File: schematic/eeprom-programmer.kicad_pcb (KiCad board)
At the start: 2 copper layers, 39.6 x 69.1 mm, 8 parts, among them IC1 AT28C64B-15PU, U1 74HC595, U2 74HC595

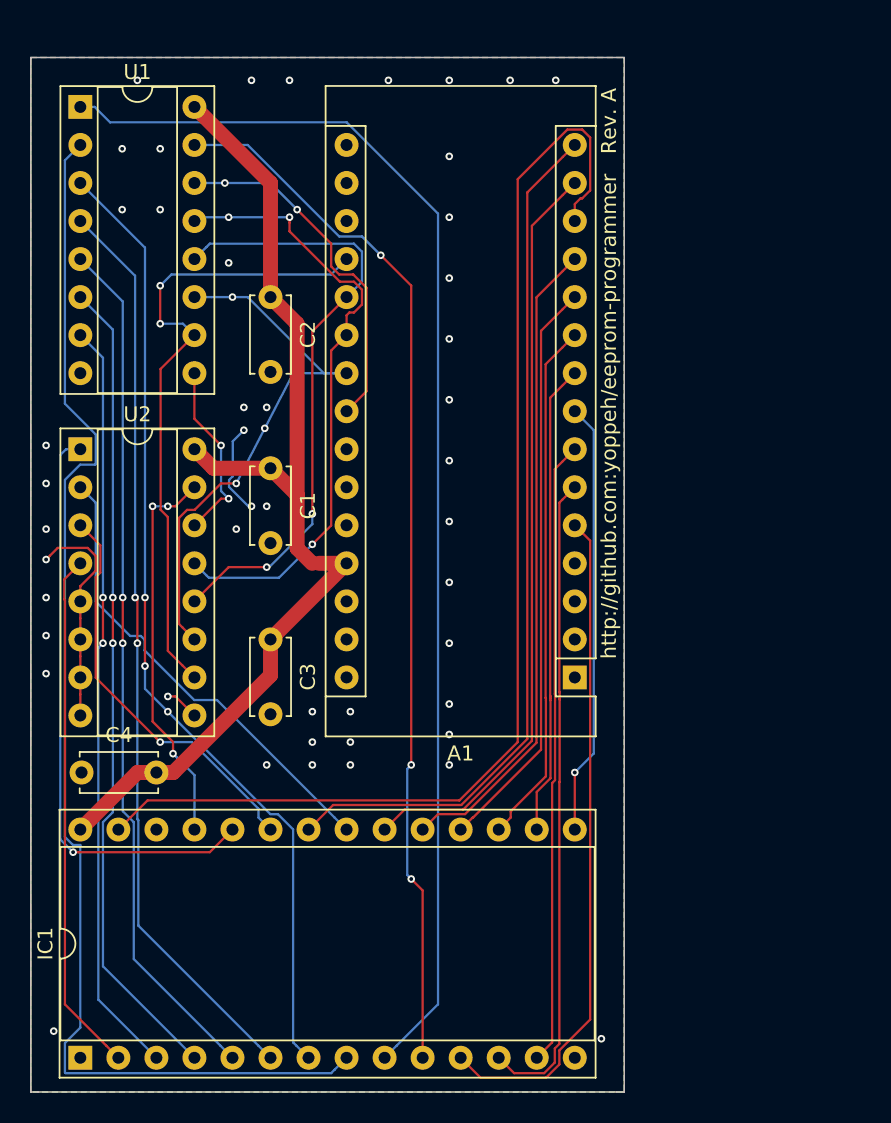
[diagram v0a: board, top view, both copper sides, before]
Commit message: Update PCB layout to handle up to 32kx8 eeproms
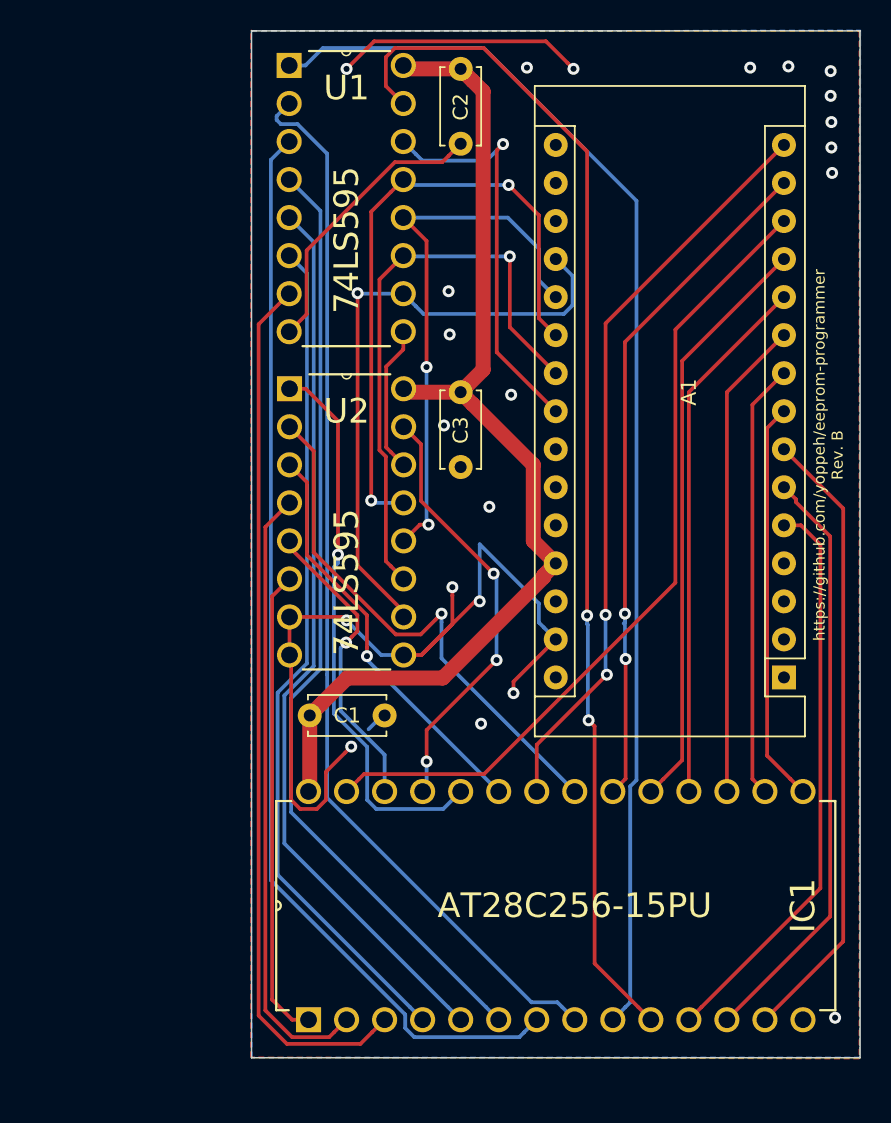
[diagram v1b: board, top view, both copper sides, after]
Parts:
- removed C4: .1uF, Capacitor_THT:C_Disc_D5.0mm_W2.5mm_P5.00mm
- A1: footprint Module:Arduino_Nano -> eeprom-programmer:Arduino_Nano
- C1, C2, C3: value .1uF -> .1uf; footprint Capacitor_THT:C_Disc_D5.0mm_W2.5mm_P5.00mm -> eeprom-programmer:C_Disc_D5.0mm_W2.5mm_P5.00mm
- IC1: value AT28C64B-15PU -> AT28C256-15PU; footprint Package_DIP:DIP-28_W15.24mm_Socket -> eeprom-programmer:DIP254P1524X482-28
- U1, U2: value 74HC595 -> 74LS595; footprint Package_DIP:DIP-16_W7.62mm_Socket -> eeprom-programmer:DIP254P762X508-16
- moved IC1 51.4 mm to (143.5, 115.6)
- moved U1 26.3 mm to (116.8, 84.9)
- moved U2 25.6 mm to (116.8, 106.5)
- moved C1 18.2 mm to (115.6, 110.5), turned to 180 degrees
- moved C3 17.1 mm to (120.7, 93.9), turned to 90 degrees
- moved C2 16.3 mm to (120.7, 72.3), turned to 90 degrees
- moved A1 14.0 mm to (142.2, 108.0)
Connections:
- A1 pad 1: (no net) -> Net-(A1-Pad1)
- A1 pad 16: (no net) -> Net-(A1-Pad16)
- A1 pad 17: (no net) -> Net-(A1-Pad17)
- A1 pad 18: (no net) -> Net-(A1-Pad18)
- A1 pad 2: (no net) -> Net-(A1-Pad2)
- A1 pad 24: (no net) -> Net-(A1-Pad24)
- A1 pad 25: (no net) -> Net-(A1-Pad25)
- A1 pad 26: (no net) -> Net-(A1-Pad26)
- A1 pad 28: (no net) -> Net-(A1-Pad28)
- A1 pad 3: (no net) -> Net-(A1-Pad3)
- A1 pad 30: (no net) -> Net-(A1-Pad30)
- A1 pad 4: (no net) -> Net-(A1-Pad4)
- C1 pad 1: Arduino5V -> GND
- C1 pad 2: GND -> Arduino5V
- C2 pad 1: Arduino5V -> GND
- C2 pad 2: GND -> Arduino5V
- C3 pad 1: Arduino5V -> GND
- C3 pad 2: GND -> Arduino5V
- IC1 pad 1: (no net) -> /addr14
- IC1 pad 26: (no net) -> /addr13
- U2 pad 5: GND -> /addr13
- U2 pad 6: GND -> /addr14
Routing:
- net GND: track 23.5 -> 94.3 mm, vias 47 -> 22
- net /addr14: track 0.00 -> 31.6 mm
- net eeNotWriteEnable: track 79.2 -> 54.9 mm
- net /addr13: track 0.00 -> 20.3 mm, vias 0 -> 1
- net /addr02: track 85.1 -> 71.4 mm
- net /addr00: track 70.5 -> 79.9 mm, vias 3 -> 2
- net /addr07: track 50.6 -> 58.9 mm, vias 2 -> 0
- net eeNotOutputEnable: track 58.1 -> 50.1 mm, vias 0 -> 2
- net /addr03: track 65.0 -> 72.9 mm, vias 3 -> 0
- net /data0: track 44.8 -> 38.3 mm
- net /addr12: track 35.0 -> 41.2 mm
- net eeNotChipEnable: track 50.7 -> 46.1 mm, vias 0 -> 2
- net srReadClock: track 41.4 -> 36.9 mm
- net /addr10: track 31.5 -> 36.0 mm, vias 0 -> 1
- net /data7: track 43.4 -> 39.2 mm
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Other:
- board size 39.6 x 69.1 mm -> 40.6 x 68.6 mm
- net class Default: clearance 0.1524 -> 0.2; trace_width 0.1534 -> 0.25; via_dia 0.508 -> 0.8; via_drill 0.254 -> 0.4
- rule trace_clearance: 0.1524 -> 0.2
- board text added: "https://github.com/yoppeh/eeprom-programmer Rev. B"
- board text removed: "http://github.com:yoppeh/eeprom-programmer Rev. A"
